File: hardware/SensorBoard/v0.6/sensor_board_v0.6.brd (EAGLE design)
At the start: 46.8 x 39.9 mm, 48 parts, among them J3 USB-MICROB, U1 ATMEGA328P, U10 CCS811, U11 RFM69HW, U2 TSL2561, U4 MPL115A, U5 FT231XS, U7 SHT31, U8 MCP1703/3.3V, U9 MCP1703CB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

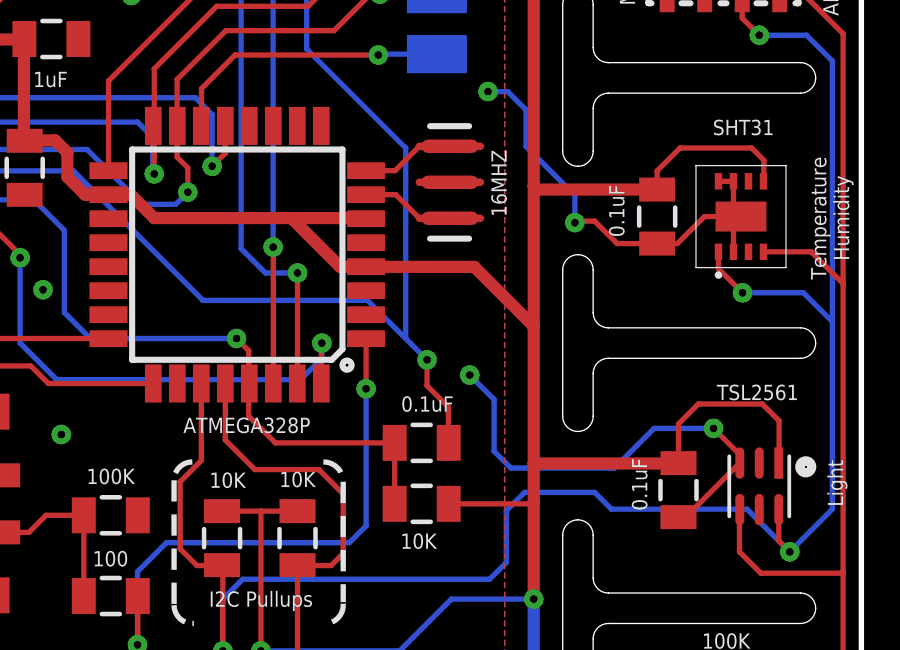
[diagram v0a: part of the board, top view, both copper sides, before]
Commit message: Adjusted a trace in sensor board
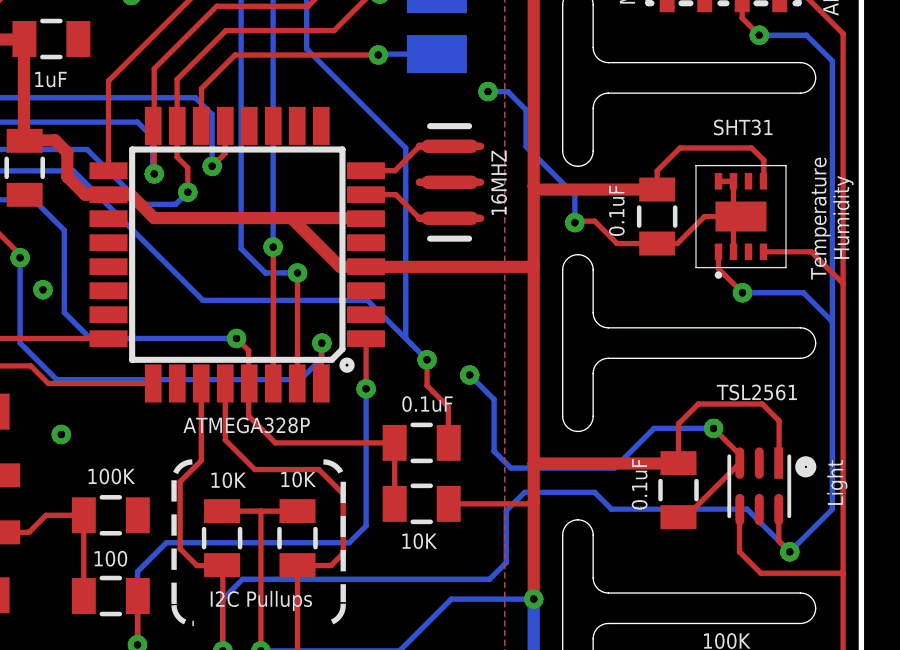
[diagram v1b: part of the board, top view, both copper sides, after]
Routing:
- net VCC: track 140.8 -> 140.0 mm
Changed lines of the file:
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@@
 <wire x1="41.7576" y1="14.6304" x2="41.7576" y2="17.8816" width="0.4064" layer="1"/>
 <wire x1="41.7576" y1="17.8816" x2="41.7576" y2="19.1516" width="0.4064" layer="1"/>
-<wire x1="41.7576" y1="19.1516" x2="41.7576" y2="23.7236" width="0.4064" layer="1"/>
-<wire x1="41.7576" y1="23.7236" x2="39.7764" y2="25.7048" width="0.4064" layer="1"/>
-<wire x1="39.7764" y1="25.7048" x2="36.176" y2="25.7048" width="0.4064" layer="1"/>
+<wire x1="41.7068" y1="25.7048" x2="36.176" y2="25.7048" width="0.4064" layer="1"/>
 <wire x1="36.176" y1="25.7048" x2="36.1696" y2="25.7112" width="0.4064" layer="1"/>
-<wire x1="41.7576" y1="23.7236" x2="41.7576" y2="28.3972" width="0.4064" layer="1"/>
+<wire x1="41.7576" y1="19.1516" x2="41.7576" y2="25.7556" width="0.4064" layer="1"/>
+<wire x1="41.7576" y1="25.7556" x2="41.7576" y2="28.3972" width="0.4064" layer="1"/>
 <wire x1="41.7576" y1="28.3972" x2="41.7576" y2="34.798" width="0.4064" layer="1"/>
 <wire x1="41.7576" y1="34.798" x2="42.5196" y2="35.56" width="0.4064" layer="1"/>
@@
 <wire x1="17.9324" y1="44.8056" x2="19.0204" y2="44.8056" width="0.1778" layer="16"/>
 <wire x1="19.0204" y1="44.8056" x2="19.0308" y2="44.7952" width="0.1778" layer="16"/>
+<wire x1="41.7068" y1="25.7048" x2="41.7576" y2="25.7556" width="0.4064" layer="1"/>
 </signal>
 <signal name="SCL">
